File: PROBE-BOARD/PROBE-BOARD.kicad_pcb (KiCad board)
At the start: 2 copper layers, 15 x 31.7 mm, 9 parts, among them J1 Conn_01x01, J2 Conn_01x01, SW1 SW_Push_Open

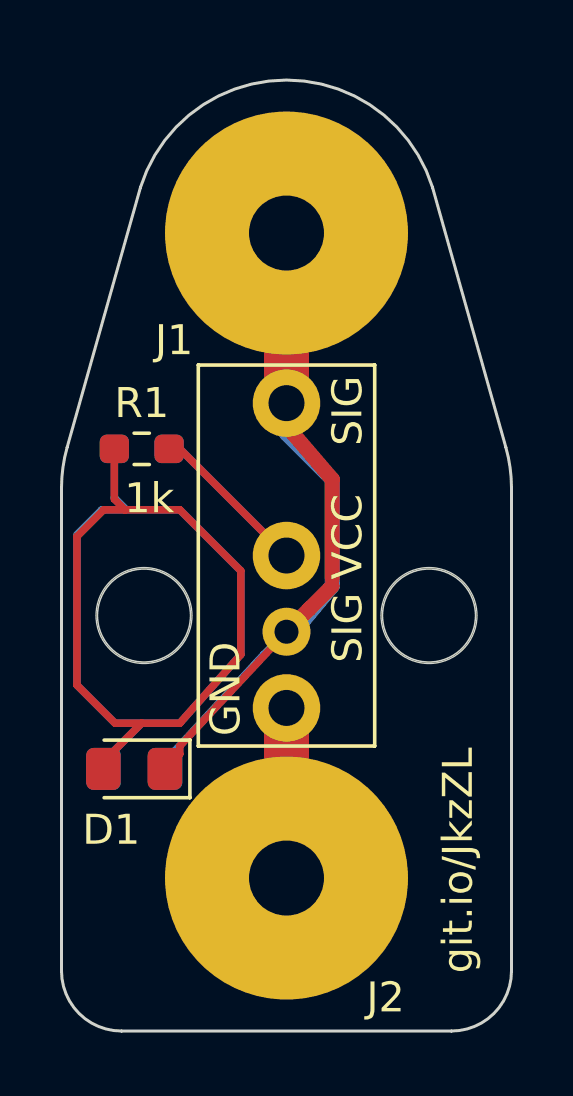
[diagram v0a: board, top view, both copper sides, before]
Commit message: updated gerbers, added XH
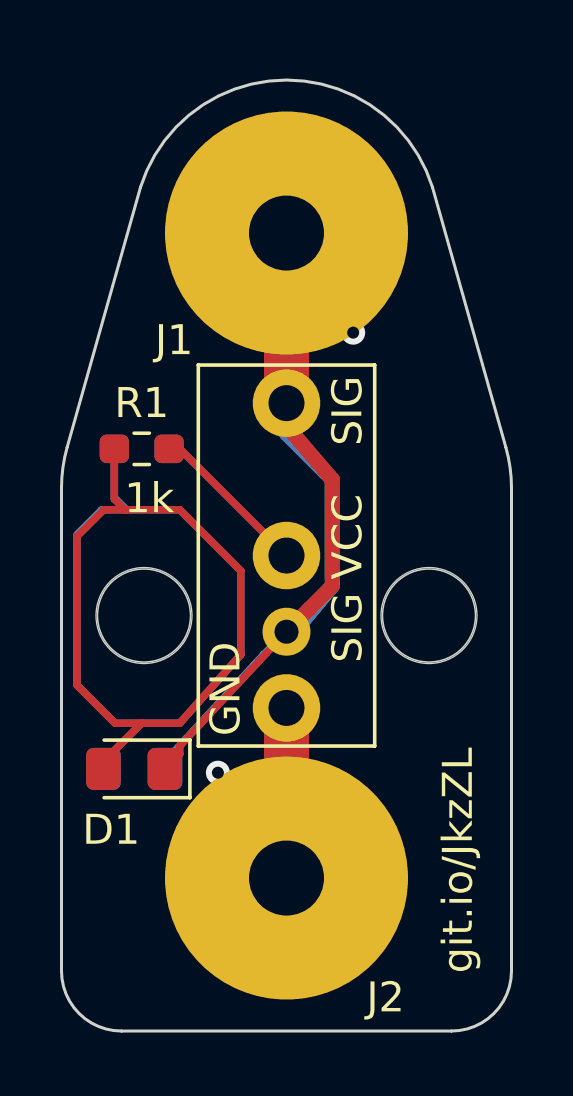
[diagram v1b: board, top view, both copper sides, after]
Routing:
- net SIGNAL: vias 0 -> 1
- net (no net): vias 0 -> 1

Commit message: move M3  mounting holes, recreted CAD, added gerbers
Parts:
- removed the REF** at (4.75, 2.00)
- removed the REF** at (-4.75, 2.00)
- added REF**: MountingHole_3.2mm_M3, MountingHole:MountingHole_3.2mm_M3, F.Cu at (5.00, -4.50)
- added REF**: MountingHole_3.2mm_M3, MountingHole:MountingHole_3.2mm_M3, F.Cu at (-5.00, -4.50)
- D1, D2: footprint LED_SMD:LED_0805_2012Metric_Pad1.15x1.40mm_HandSolder -> LED_SMD:LED_1206_3216Metric_Pad1.42x1.75mm_HandSolder
- R1, R2: footprint Resistor_SMD:R_0603_1608Metric_Pad0.98x0.95mm_HandSolder -> Resistor_SMD:R_1206_3216Metric_Pad1.30x1.75mm_HandSolder
- moved R1 4.27 mm to (-4.95, 0.71)
- moved R2 4.26 mm to (-4.95, 0.70)
- moved D2 1.99 mm to (-4.63, 5.17), turned to 90 degrees
- moved D1 1.93 mm to (-4.63, 5.23), turned to 90 degrees
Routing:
- net Net-(D2-Pad2): track 25.7 -> 3.76 mm
- net Net-(D1-Pad2): track 25.8 -> 4.28 mm
- net VCC: track 11.0 -> 7.79 mm
- net SIGNAL: track 44.5 -> 46.8 mm
- net GND: vias 0 -> 1
- net (no net): vias 1 -> 0
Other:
- outline, holes or cut-outs redrawn

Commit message: bOARD rev2
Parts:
- added REF**: JST-XH, mag-probe:JST-XH, F.Cu at (0.00, 0.00)
- added REF**: M3Heatsrt, mag-probe:M3Heatsrt, F.Cu at (-4.45, -5.80)
- added REF**: M3Heatsrt, mag-probe:M3Heatsrt, F.Cu at (4.45, -5.85)
- moved REF** 1.35 mm to (4.50, -5.75)
- moved REF** 1.31 mm to (-4.60, -5.75)
